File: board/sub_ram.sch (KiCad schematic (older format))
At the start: 0 parts

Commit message: RAM Done
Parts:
- added C?: 1u, symbol Device:C
- added U?: AS6C8008, symbol quokka:AS6C8008
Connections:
- net 6502_R~W: now also U?.17 (WE#)
- net RAM_~cs: now also U?.6 (CE#)
- new net +5V: C?.1, U?.11 (Vcc), U?.33 (Vcc), U?.40 (CE2)
- new net A0: U?.5 (A0)
- new net A1: U?.4 (A1)
- new net A10: U?.27 (A10)
- new net A11: U?.26 (A11)
- new net A12: U?.25 (A12)
- new net A13: U?.24 (A13)
- new net A14: U?.23 (A14)
- new net A15: U?.22 (A15)
- new net A16: U?.21 (A16)
- new net A17: U?.20 (A17)
- new net A18: U?.19 (A18)
- new net A19: U?.18 (A19)
- new net A2: U?.3 (A2)
- new net A3: U?.2 (A3)
- new net A4: U?.1 (A4)
- new net A5: U?.44 (A5)
- new net A6: U?.43 (A6)
- new net A7: U?.42 (A7)
- new net A8: U?.39 (A8)
- new net A9: U?.28 (A9)
- new net D0: U?.9 (DQ0)
- new net D1: U?.10 (DQ1)
- new net D2: U?.13 (DQ2)
- new net D3: U?.14 (DQ3)
- new net D4: U?.31 (DQ4)
- new net D5: U?.32 (DQ5)
- new net D6: U?.35 (DQ6)
- new net D7: U?.36 (DQ7)
- new net GND: C?.2, U?.12 (Vss), U?.34 (Vss), U?.41 (OE#)

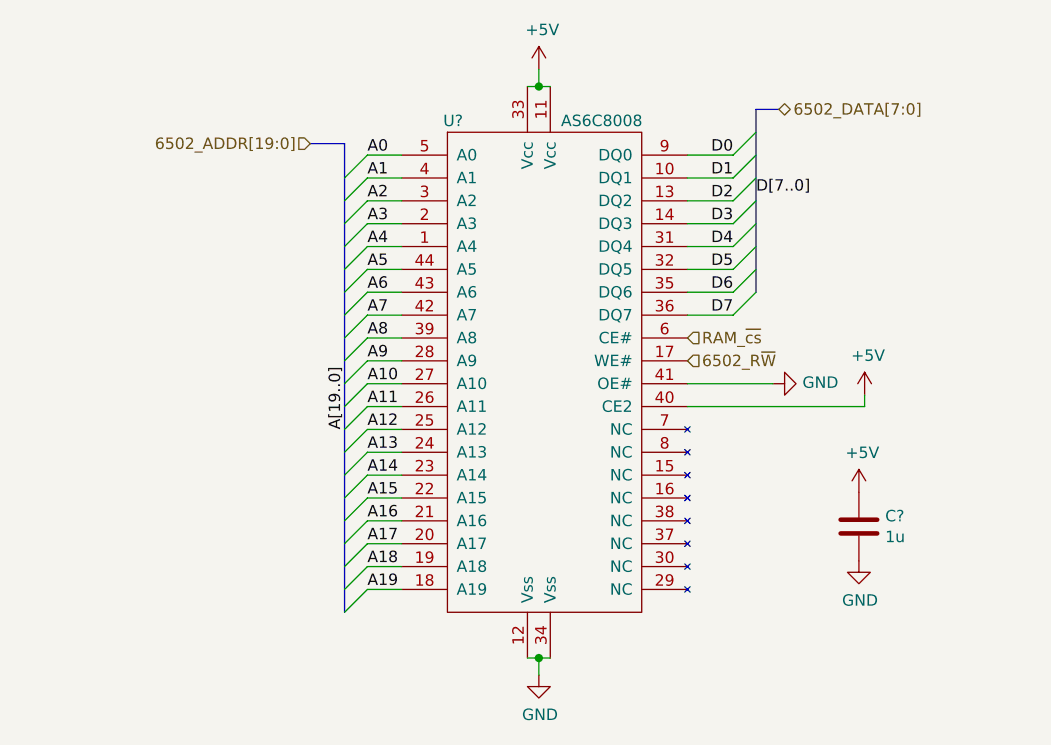
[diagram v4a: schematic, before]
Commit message: made some changes based on projected power budget
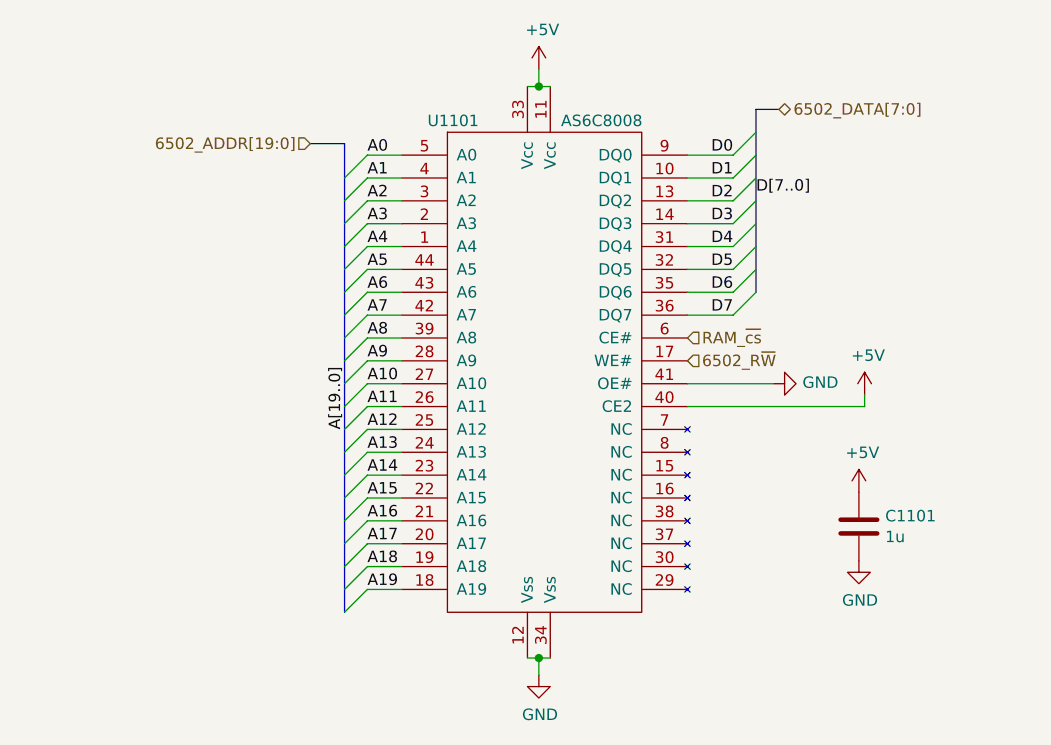
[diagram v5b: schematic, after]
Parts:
- gave numbers to parts that had none: 2
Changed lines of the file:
@@
 RAM_~cs
 $Comp
-L quokka:AS6C8008 U?
+L quokka:AS6C8008 U1101
 U 1 1 5AACCF3F
 P 5400 2675
-F 0 "U?" H 4975 3825 50  0000 C CNN
+F 0 "U1101" H 4975 3825 50  0000 C CNN
 F 1 "AS6C8008" H 5625 3825 50  0000 C CNN
 F 2 "" H 5000 3125 50  0001 C CNN
@@
 D[7..0]
 $Comp
-L power:GND #PWR?
+L power:GND #PWR01103
 U 1 1 5AADD2F2
 P 6375 2675
-F 0 "#PWR?" H 6375 2425 50  0001 C CNN
+F 0 "#PWR01103" H 6375 2425 50  0001 C CNN
 F 1 "GND" V 6380 2547 50  0000 R CNN
 F 2 "" H 6375 2675 50  0001 C CNN
@@
 $EndComp
 $Comp
-L power:+5V #PWR?
+L power:+5V #PWR01106
 U 1 1 5AADD352
 P 6775 2725
-F 0 "#PWR?" H 6775 2575 50  0001 C CNN
+F 0 "#PWR01106" H 6775 2575 50  0001 C CNN
 F 1 "+5V" H 6790 2898 50  0000 C CNN
 F 2 "" H 6775 2725 50  0001 C CNN
@@
 	6000 2675 6375 2675
 $Comp
-L power:+5V #PWR?
+L power:+5V #PWR01101
 U 1 1 5AADE4E9
 P 5350 1300
-F 0 "#PWR?" H 5350 1150 50  0001 C CNN
+F 0 "#PWR01101" H 5350 1150 50  0001 C CNN
 F 1 "+5V" H 5365 1473 50  0000 C CNN
 F 2 "" H 5350 1300 50  0001 C CNN
@@
 $EndComp
 $Comp
-L power:GND #PWR?
+L power:GND #PWR01102
 U 1 1 5AADE4F6
 P 5350 3950
-F 0 "#PWR?" H 5350 3700 50  0001 C CNN
+F 0 "#PWR01102" H 5350 3700 50  0001 C CNN
 F 1 "GND" H 5355 3777 50  0000 C CNN
 F 2 "" H 5350 3950 50  0001 C CNN
@@
 Connection ~ 5350 3875
 $Comp
-L Device:C C?
+L Device:C C1101
 U 1 1 5AAE269C
 P 6750 3300
-F 0 "C?" H 6865 3346 50  0000 L CNN
+F 0 "C1101" H 6865 3346 50  0000 L CNN
 F 1 "1u" H 6865 3255 50  0000 L CNN
 F 2 "" H 6788 3150 50  0001 C CNN
@@
 $EndComp
 $Comp
-L power:GND #PWR?
+L power:GND #PWR01105
 U 1 1 5AAE26A3
 P 6750 3450
-F 0 "#PWR?" H 6750 3200 50  0001 C CNN
+F 0 "#PWR01105" H 6750 3200 50  0001 C CNN
 F 1 "GND" H 6755 3277 50  0000 C CNN
 F 2 "" H 6750 3450 50  0001 C CNN
@@
 $EndComp
 $Comp
-L power:+5V #PWR?
+L power:+5V #PWR01104
 U 1 1 5AAE26A9
 P 6750 3150
-F 0 "#PWR?" H 6750 3000 50  0001 C CNN
+F 0 "#PWR01104" H 6750 3000 50  0001 C CNN
 F 1 "+5V" H 6765 3323 50  0000 C CNN
 F 2 "" H 6750 3150 50  0001 C CNN

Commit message: Schematics mostly complete
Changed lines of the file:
@@
 $EndDescr
 Text HLabel 6400 1475 2    50   3State ~ 0
-6502_DATA[7:0]
+6502_DATA[7..0]
 Text HLabel 4350 1625 0    50   Input ~ 0
-6502_ADDR[19:0]
+6502_ADDR[19..0]
 Text HLabel 6000 2575 2    50   Input ~ 0
 6502_R~W
@@
 D[7..0]
 $Comp
-L power:GND #PWR01103
+L power:GND #PWR01102
 U 1 1 5AADD2F2
 P 6375 2675
-F 0 "#PWR01103" H 6375 2425 50  0001 C CNN
+F 0 "#PWR01102" H 6375 2425 50  0001 C CNN
 F 1 "GND" V 6380 2547 50  0000 R CNN
 F 2 "" H 6375 2675 50  0001 C CNN
@@
 $EndComp
 $Comp
-L power:+5V #PWR01106
+L power:+5V #PWR01103
 U 1 1 5AADD352
 P 6775 2725
-F 0 "#PWR01106" H 6775 2575 50  0001 C CNN
+F 0 "#PWR01103" H 6775 2575 50  0001 C CNN
 F 1 "+5V" H 6790 2898 50  0000 C CNN
 F 2 "" H 6775 2725 50  0001 C CNN
@@
 $EndComp
 $Comp
-L power:GND #PWR01102
+L power:GND #PWR01106
 U 1 1 5AADE4F6
 P 5350 3950
-F 0 "#PWR01102" H 5350 3700 50  0001 C CNN
+F 0 "#PWR01106" H 5350 3700 50  0001 C CNN
 F 1 "GND" H 5355 3777 50  0000 C CNN
 F 2 "" H 5350 3950 50  0001 C CNN

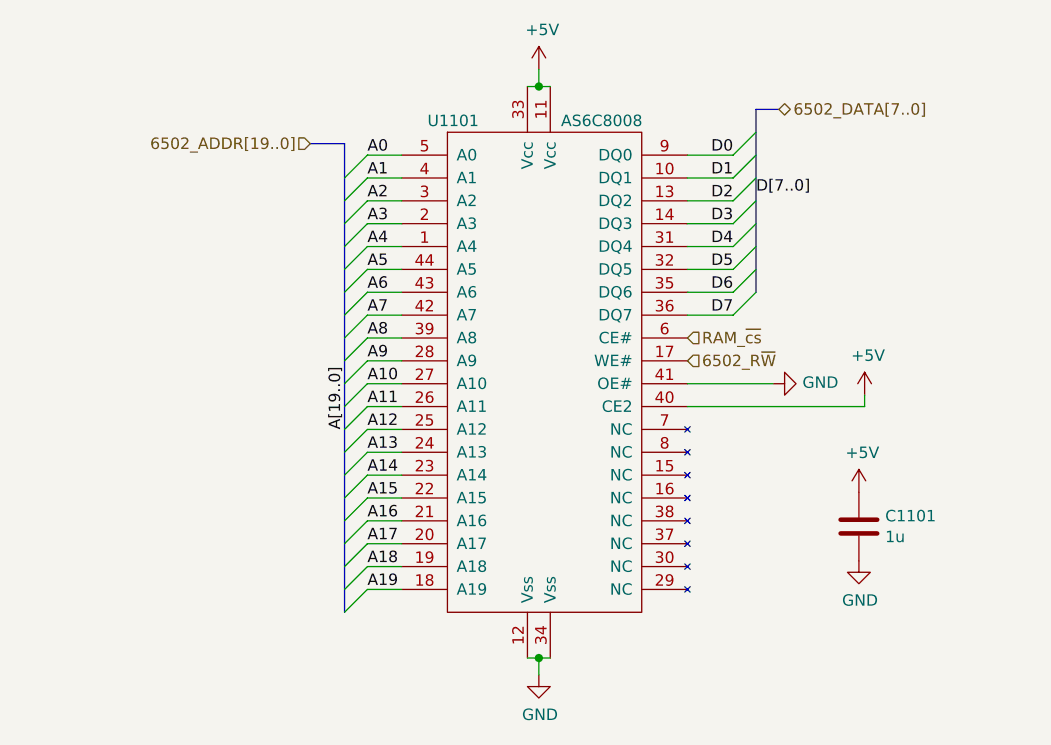
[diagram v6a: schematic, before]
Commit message: Started picking footprints. Merged many components.
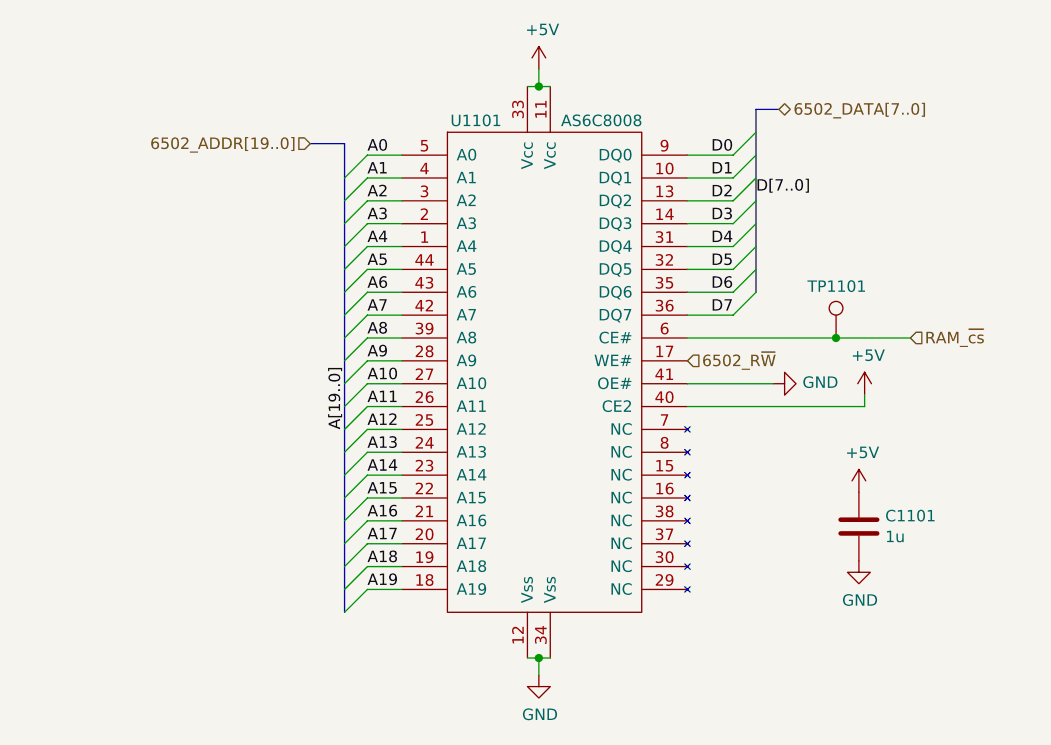
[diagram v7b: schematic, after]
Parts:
- added TP1101: Test_Point, TestPoint:TestPoint_Plated_Hole_D2.0mm, symbol Connector_Specialized:Test_Point
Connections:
- net RAM_~cs: now also TP1101.1
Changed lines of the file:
@@
 $Descr A4 11693 8268
 encoding utf-8
-Sheet 11 14
+Sheet 11 15
 Title ""
 Date ""
@@
 Text HLabel 6000 2575 2    50   Input ~ 0
 6502_R~W
-Text HLabel 6000 2475 2    50   Input ~ 0
+Text HLabel 6975 2475 2    50   Input ~ 0
 RAM_~cs
 $Comp
@@
 U 1 1 5AACCF3F
 P 5400 2675
-F 0 "U1101" H 4975 3825 50  0000 C CNN
+F 0 "U1101" H 5075 3825 50  0000 C CNN
 F 1 "AS6C8008" H 5625 3825 50  0000 C CNN
 F 2 "" H 5000 3125 50  0001 C CNN
@@
 	1    0    0    -1
 $EndComp
+Wire Wire Line
+	6000 2475 6650 2475
+$Comp
+L Connector_Specialized:Test_Point TP1101
+U 1 1 5ABC743D
+P 6650 2475
+F 0 "TP1101" H 6525 2700 50  0000 L CNN
+F 1 "Test_Point" H 6708 2504 50  0001 L CNN
+F 2 "TestPoint:TestPoint_Plated_Hole_D2.0mm" H 6850 2475 50  0001 C CNN
+F 3 "~" H 6850 2475 50  0001 C CNN
+	1    6650 2475
+	1    0    0    -1
+$EndComp
+Connection ~ 6650 2475
+Wire Wire Line
+	6650 2475 6975 2475
 Wire Bus Line
 	6300 1475 6300 2275

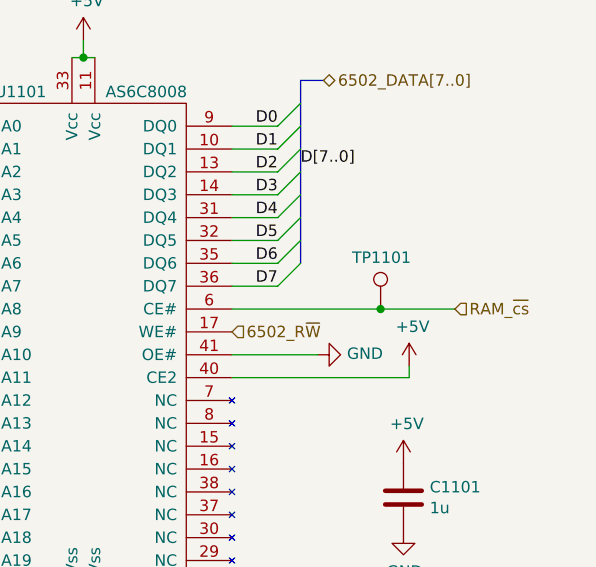
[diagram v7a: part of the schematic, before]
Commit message: More footprints done. Went with simpler test-pads.
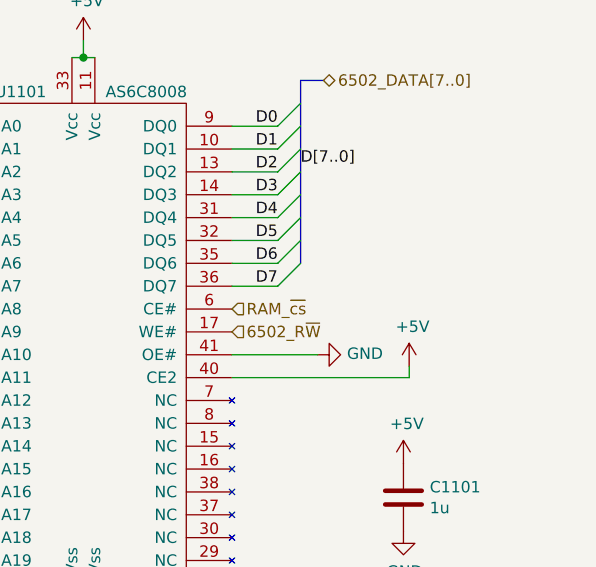
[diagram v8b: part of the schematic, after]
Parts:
- removed TP1101: Test_Point, TestPoint:TestPoint_Plated_Hole_D2.0mm, symbol Connector_Specialized:Test_Point
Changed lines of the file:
@@
 $Descr A4 11693 8268
 encoding utf-8
-Sheet 11 15
+Sheet 11 14
 Title ""
 Date ""
@@
 Text HLabel 6000 2575 2    50   Input ~ 0
 6502_R~W
-Text HLabel 6975 2475 2    50   Input ~ 0
+Text HLabel 6000 2475 2    50   Input ~ 0
 RAM_~cs
 $Comp
@@
 	1    0    0    -1
 $EndComp
-Wire Wire Line
-	6000 2475 6650 2475
-$Comp
-L Connector_Specialized:Test_Point TP1101
-U 1 1 5ABC743D
-P 6650 2475
-F 0 "TP1101" H 6525 2700 50  0000 L CNN
-F 1 "Test_Point" H 6708 2504 50  0001 L CNN
-F 2 "TestPoint:TestPoint_Plated_Hole_D2.0mm" H 6850 2475 50  0001 C CNN
-F 3 "~" H 6850 2475 50  0001 C CNN
-	1    6650 2475
-	1    0    0    -1
-$EndComp
-Connection ~ 6650 2475
-Wire Wire Line
-	6650 2475 6975 2475
 Wire Bus Line
 	6300 1475 6300 2275
